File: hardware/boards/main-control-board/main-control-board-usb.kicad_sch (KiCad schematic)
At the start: 3 parts

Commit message: integrate PCA into the board
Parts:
- R1, R2: FT Rotation Offset 90 -> (none)
- USB1: FT Rotation Offset 90 -> (none); LCSC Part C2765186 -> (none)
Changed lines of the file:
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@@
-			)
-		)
-		(property "FT Rotation Offset" "90"
-			(at 107.95 66.04 90)
-			(hide yes)
-			(show_name no)
-			(do_not_autoplace no)
-			(effects
-				(font
-					(size 1.27 1.27)
-				)
 			)
 		)
@@
 			)
 		)
-		(property "FT Rotation Offset" "90"
-			(at 135.89 74.93 0)
-			(hide yes)
-			(show_name no)
-			(do_not_autoplace no)
-			(effects
-				(font
-					(size 1.27 1.27)
-				)
-			)
-		)
-		(property "LCSC Part" "C2765186"
-			(at 135.89 106.68 0)
-			(hide yes)
-			(show_name no)
-			(do_not_autoplace no)
-			(effects
-				(font
-					(size 1.27 1.27)
-				)
-			)
-		)
 		(pin "B7"
 		)
@@
 			(at 107.95 83.82 90)
 			(hide yes)
-			(show_name no)
-			(do_not_autoplace no)
-			(effects
-				(font
-					(size 1.27 1.27)
-				)
-			)
-		)
-		(property "FT Rotation Offset" "90"
-			(at 107.95 83.82 90)
-			(hide yes)

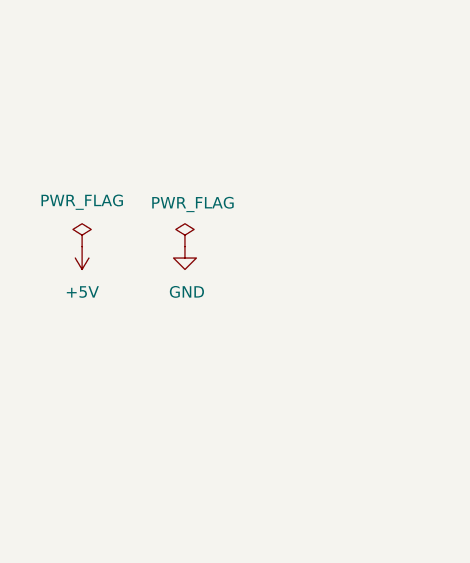
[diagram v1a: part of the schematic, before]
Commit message: add power indicator
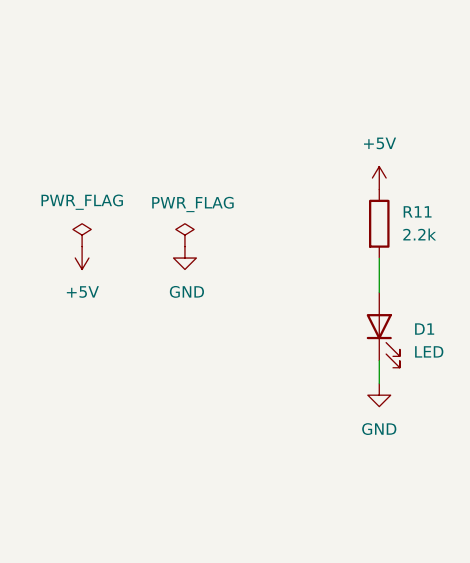
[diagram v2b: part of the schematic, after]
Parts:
- added D1: LED, LED_SMD:LED_0603_1608Metric, symbol Device:LED
- added R11: 2.2k, Resistor_SMD:R_0603_1608Metric, symbol Device:R
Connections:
- net +5V: now also R11.1
- net GND: now also D1.1 (K)
- new net: D1.2 (A), R11.2

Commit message: use basic components over extended
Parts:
- D1: LCSC Part # C965804 -> C2286
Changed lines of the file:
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@@
 			)
 		)
-		(property "LCSC Part #" "C965804"
+		(property "LCSC Part #" "C2286"
 			(at 205.74 83.82 90)
 			(hide yes)

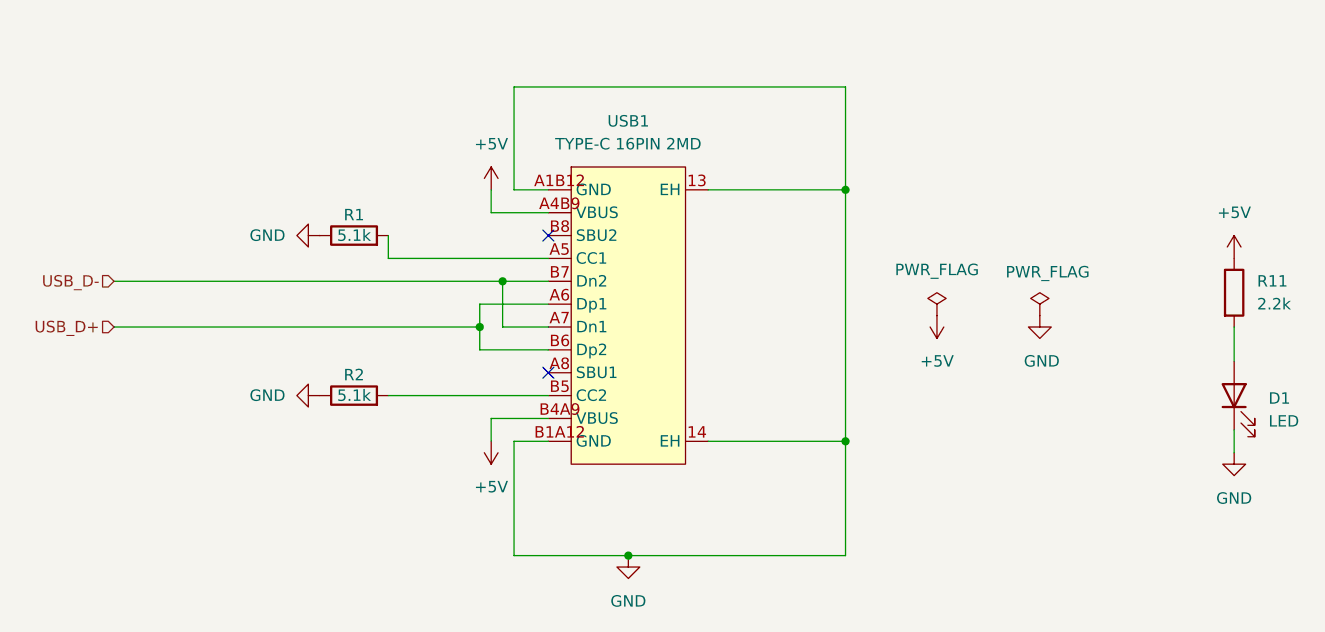
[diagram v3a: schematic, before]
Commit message: add polyfuse protection
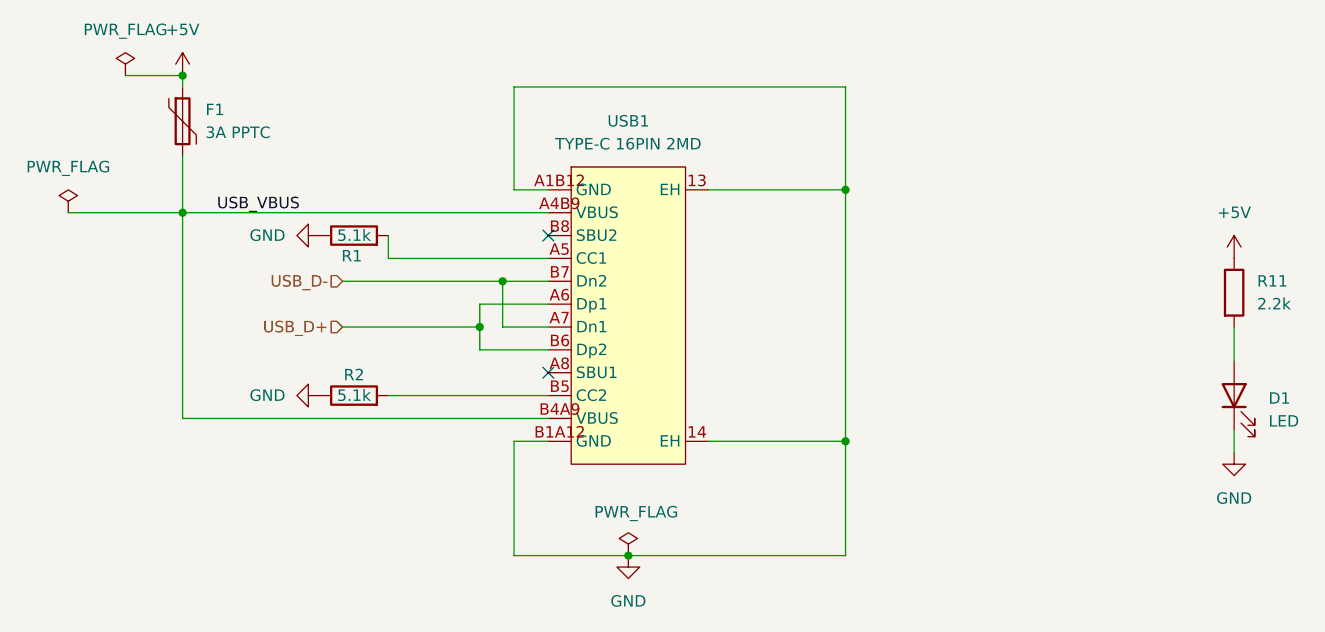
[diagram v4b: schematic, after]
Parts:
- added F1: 3A PPTC, Fuse:Fuse_1812_4532Metric, symbol Device:Polyfuse
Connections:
- net +5V: now also F1.1; no longer USB1.A4B9 (VBUS), USB1.B4A9 (VBUS)
- new net USB_VBUS: F1.2, USB1.A4B9 (VBUS), USB1.B4A9 (VBUS)

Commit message: pre-fab improvements
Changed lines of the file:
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@@
 	)
 	(hierarchical_label "USB_D-"
-		(shape input)
+		(shape bidirectional)
 		(at 106.68 71.12 180)
 		(effects
@@
 	)
 	(hierarchical_label "USB_D+"
-		(shape input)
+		(shape bidirectional)
 		(at 106.68 76.2 180)
 		(effects

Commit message: feat(pcb): update component properties and add missing attributes
- Renamed connection values for ESP32 components to standardize naming.
- Added properties for KiLib_Generator, MPN, and Manufacturer for various components across multiple schematic files.
- Enhanced documentation for component attributes to improve clarity and accessibility in the design process.
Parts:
- D1: MPN (none) -> KT-0603R; Manufacturer (none) -> Hubei KENTO Elec
- F1: MPN (none) -> BSMD1812-300-16V; Manufacturer (none) -> BHFUSE
- R1, R2: MPN (none) -> 0603WAF5101T5E; Manufacturer (none) -> UNI-ROYAL(Uniroyal Elec)
- R11: MPN (none) -> 0603WAF2201T5E; Manufacturer (none) -> UNI-ROYAL(Uniroyal Elec)
- USB1: Manufacturer SHOU HAN(首韩) -> SHOU HAN
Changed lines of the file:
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@@
+			)
+		)
+		(property "KiLib_Generator" ""
+			(at 107.95 66.04 90)
+			(hide yes)
+			(show_name no)
+			(do_not_autoplace no)
+			(effects
+				(font
+					(size 1.27 1.27)
+				)
+			)
+		)
+		(property "MPN" "0603WAF5101T5E"
+			(at 107.95 66.04 90)
+			(hide yes)
+			(show_name no)
+			(do_not_autoplace no)
+			(effects
+				(font
+					(size 1.27 1.27)
+				)
+			)
+		)
+		(property "Manufacturer" "UNI-ROYAL(Uniroyal Elec)"
+			(at 107.95 66.04 90)
+			(hide yes)
+			(show_name no)
+			(do_not_autoplace no)
+			(effects
+				(font
+					(size 1.27 1.27)
+				)
 			)
 		)
@@
 			)
 		)
-		(property "Manufacturer" "SHOU HAN(首韩)"
+		(property "Manufacturer" "SHOU HAN"
 			(at 135.89 101.6 0)
 			(hide yes)
@@
 		(property "LCSC Part #" "C2765186"
 			(at 135.89 106.68 0)
+			(hide yes)
+			(show_name no)
+			(do_not_autoplace no)
+			(effects
+				(font
+					(size 1.27 1.27)
+				)
+			)
+		)
+		(property "KiLib_Generator" ""
+			(at 135.89 74.93 0)
 			(hide yes)
 			(show_name no)
@@
 			)
 		)
+		(property "KiLib_Generator" ""
+			(at 88.9 53.34 0)
+			(hide yes)
+			(show_name no)
+			(do_not_autoplace no)
+			(effects
+				(font
+					(size 1.27 1.27)
+				)
+			)
+		)
+		(property "MPN" "BSMD1812-300-16V"
+			(at 88.9 53.34 0)
+			(hide yes)
+			(show_name no)
+			(do_not_autoplace no)
+			(effects
+				(font
+					(size 1.27 1.27)
+				)
+			)
+		)
+		(property "Manufacturer" "BHFUSE"
+			(at 88.9 53.34 0)
+			(hide yes)
+			(show_name no)
+			(do_not_autoplace no)
+			(effects
+				(font
+					(size 1.27 1.27)
+				)
+			)
+		)
 		(pin "1"
 		)
@@
 		)
 		(property "LCSC Part #" "C23186"
+			(at 107.95 83.82 90)
+			(hide yes)
+			(show_name no)
+			(do_not_autoplace no)
+			(effects
+				(font
+					(size 1.27 1.27)
+				)
+			)
+		)
+		(property "KiLib_Generator" ""
+			(at 107.95 83.82 90)
+			(hide yes)
+			(show_name no)
+			(do_not_autoplace no)
+			(effects
+				(font
+					(size 1.27 1.27)
+				)
+			)
+		)
+		(property "MPN" "0603WAF5101T5E"
+			(at 107.95 83.82 90)
+			(hide yes)
+			(show_name no)
+			(do_not_autoplace no)
+			(effects
+				(font
+					(size 1.27 1.27)
+				)
+			)
+		)
+		(property "Manufacturer" "UNI-ROYAL(Uniroyal Elec)"
 			(at 107.95 83.82 90)
 			(hide yes)
@@
 			)
 		)
+		(property "KiLib_Generator" ""
+			(at 205.74 83.82 90)
+			(hide yes)
+			(show_name no)
+			(do_not_autoplace no)
+			(effects
+				(font
+					(size 1.27 1.27)
+				)
+			)
+		)
+		(property "MPN" "KT-0603R"
+			(at 205.74 83.82 90)
+			(hide yes)
+			(show_name no)
+			(do_not_autoplace no)
+			(effects
+				(font
+					(size 1.27 1.27)
+				)
+			)
+		)
+		(property "Manufacturer" "Hubei KENTO Elec"
+			(at 205.74 83.82 90)
+			(hide yes)
+			(show_name no)
+			(do_not_autoplace no)
+			(effects
+				(font
+					(size 1.27 1.27)
+				)
+			)
+		)
 		(pin "1"
 		)
@@
 			(at 205.74 72.39 0)
 			(hide yes)
+			(show_name no)
+			(do_not_autoplace no)
+			(effects
+				(font
+					(size 1.27 1.27)
+				)
+			)
+		)
+		(property "KiLib_Generator" ""
+			(at 205.74 72.39 0)
+			(hide yes)
+			(show_name no)
+			(do_not_autoplace no)
+			(effects
+				(font
+					(size 1.27 1.27)
+				)
+			)
+		)
+		(property "MPN" "0603WAF2201T5E"
+			(at 205.74 72.39 0)
+			(hide yes)
+			(show_name no)
+			(do_not_autoplace no)
+			(effects
+				(font
+					(size 1.27 1.27)
+				)
+			)
+		)
+		(property "Manufacturer" "UNI-ROYAL(Uniroyal Elec)"
+			(at 205.74 72.39 0)
+			(hide yes)
